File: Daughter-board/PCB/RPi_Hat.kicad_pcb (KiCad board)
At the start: 2 copper layers, 65 x 56.5 mm, 20 parts, among them J1 Conn_01x05, J2 RPi_GPIO, J3 Conn_01x05, J4 Conn_01x05, J5 Conn_01x07, J6 Conn_01x07, J7 Conn_01x05, J8 Conn_02x07_Odd_Even, J9 Conn_01x04, Q1 2N7002, Q2 2N7002, Q3 2N7002

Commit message: update psu and hat
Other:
- board text added: "Hydro B. HAT"
- board text added: "Hydro B. PSU"
- board text removed: "PSU"
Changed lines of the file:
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@@
-(kicad_pcb (version 20171130) (host pcbnew 5.0.2+dfsg1-1~bpo9+1)
+(kicad_pcb (version 20171130) (host pcbnew "(5.1.5)-3")
   (general
     (thickness 1.6)
-    (drawings 37)
+    (drawings 38)
     (tracks 145)
     (zones 0)
@@
     (zone_45_only no)
     (trace_min 0)
-    (segment_width 0.2)
-    (edge_width 0.1)
     (via_size 0.6)
     (via_drill 0.4)
@@
     (uvia_min_size 0.2)
     (uvia_min_drill 0.1)
+    (edge_width 0.1)
+    (segment_width 0.2)
     (pcb_text_width 0.3)
     (pcb_text_size 1.5 1.5)
@@
       (solder_mask_margin 1.725) (clearance 1.725))
   )
-  (gr_text PSU (at 149.86 80.01 90) (layer F.SilkS)
+  (gr_text "Hydro B. HAT" (at 135.255 118.745) (layer F.SilkS)
+    (effects (font (size 3 3) (thickness 0.5)))
+  )
+  (gr_text "Hydro B. PSU" (at 149.86 83.82 90) (layer F.SilkS)
     (effects (font (size 1 1) (thickness 0.15)))
   )
-  (gr_text I2C (at 142.875 111.76 90) (layer F.SilkS)
+  (gr_text I2C (at 142.875 98.425 90) (layer F.SilkS)
     (effects (font (size 1 1) (thickness 0.15)))
   )
-  (gr_text I2C (at 135.255 111.76 90) (layer F.SilkS)
+  (gr_text I2C (at 135.255 98.425 90) (layer F.SilkS)
     (effects (font (size 1 1) (thickness 0.15)))
   )
-  (gr_text I2C (at 127.635 111.76 90) (layer F.SilkS)
+  (gr_text I2C (at 127.635 98.425 90) (layer F.SilkS)
     (effects (font (size 1 1) (thickness 0.15)))
   )

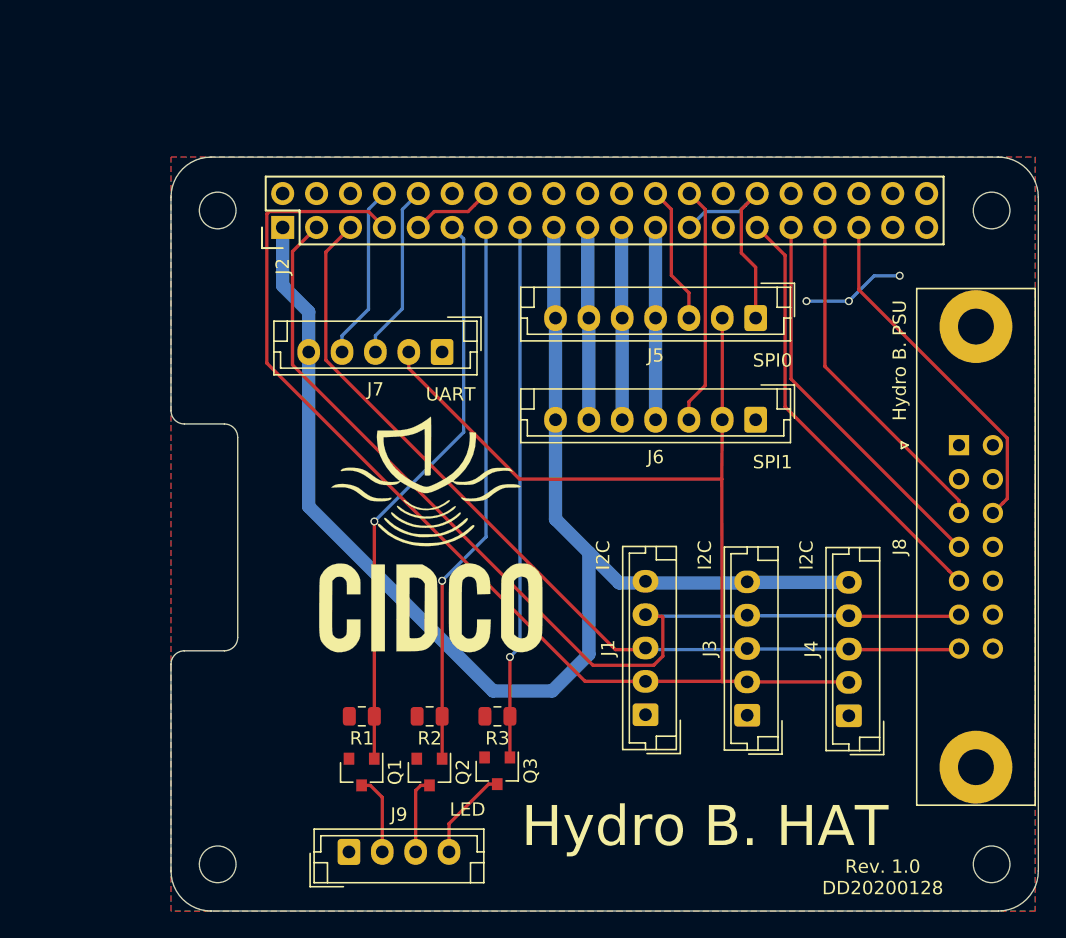
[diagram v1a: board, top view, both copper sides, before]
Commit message: smt to TH
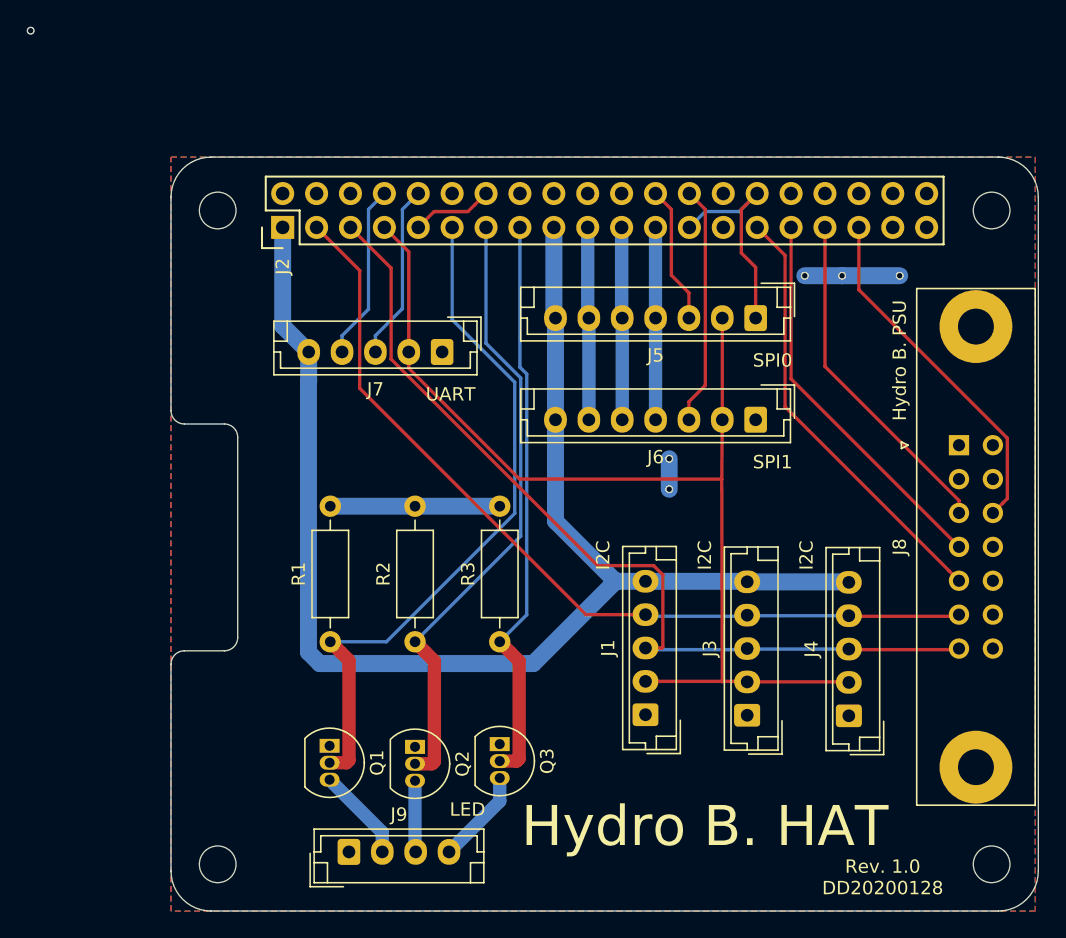
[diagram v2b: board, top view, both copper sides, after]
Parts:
- removed the ? at (156.8, 72.6)
- removed the ? at (156.8, 121.6)
- removed the ? at (98.8, 121.6)
- removed the ? at (98.8, 72.6)
- removed G***: LOGO, cidco:logo cidco
- added ?: , cidco:MountingHole_2.7mm_M2.5_Pad, F.Cu at (98.8, 121.6)
- added ?: , cidco:MountingHole_2.7mm_M2.5_Pad, F.Cu at (156.8, 121.6)
- added ?: , cidco:MountingHole_2.7mm_M2.5_Pad, F.Cu at (156.8, 72.6)
- added ?: , cidco:MountingHole_2.7mm_M2.5_Pad, F.Cu at (98.8, 72.6)
- J2: footprint RPi_Hat:Pin_Header_Straight_2x20 -> cidco:Pin_Header_Straight_2x20
- Q1, Q2, Q3: value 2N7002 -> 2N7000; footprint Package_TO_SOT_SMD:SOT-23 -> Package_TO_SOT_THT:TO-92_Inline
- R1, R2, R3: value R_US -> 1k; footprint Resistor_SMD:R_0805_2012Metric -> Resistor_THT:R_Axial_DIN0207_L6.3mm_D2.5mm_P10.16mm_Horizontal
- moved R1 6.07 mm to (107.2, 104.9), turned to 90 degrees
- moved R2 5.69 mm to (113.5, 104.9), turned to 90 degrees
- moved R3 5.59 mm to (119.9, 104.9), turned to 90 degrees
- moved Q1 3.10 mm to (107.1, 112.7)
- moved Q2 2.18 mm to (113.5, 112.8)
- moved Q3 2.01 mm to (119.9, 112.6)
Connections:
- Q1 pad 1: LEDR -> GND
- Q1 pad 2: GND -> LEDR
- Q2 pad 1: LEDG -> GND
- Q2 pad 2: GND -> LEDG
- Q3 pad 1: LEDB -> GND
- Q3 pad 2: GND -> LEDB
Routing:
- net PPS: track 129.5 -> 80.7 mm
- net GND: track 30.3 -> 44.6 mm, vias 3 -> 5
- net SDA: track 76.2 -> 65.4 mm
- net LEDR: track 42.9 -> 52.2 mm, vias 1 -> 0
- net LEDG: track 41.2 -> 46.5 mm, vias 1 -> 0
- net LEDB: track 40.0 -> 43.0 mm, vias 1 -> 0
- net 3.3V: track 103.1 -> 104.5 mm
- net SCL: track 67.2 -> 68.5 mm
- net Net-(J9-Pad2): track 6.01 -> 7.05 mm
- net (no net): vias 0 -> 1

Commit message: update
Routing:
- net (no net): vias 1 -> 0
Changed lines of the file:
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@@
-(kicad_pcb (version 20171130) (host pcbnew "(5.1.5)-3")
+(kicad_pcb (version 20171130) (host pcbnew 5.0.2+dfsg1-1~bpo9+1)
   (general
     (thickness 1.6)
     (drawings 38)
-    (tracks 152)
+    (tracks 151)
     (zones 0)
     (modules 19)
@@
   )
   (setup
-    (last_trace_width 1.27)
+    (last_trace_width 0.25)
     (user_trace_width 0.01)
     (user_trace_width 0.02)
@@
     (zone_45_only no)
     (trace_min 0)
+    (segment_width 0.2)
+    (edge_width 0.1)
     (via_size 0.6)
     (via_drill 0.4)
@@
     (uvia_min_size 0.2)
     (uvia_min_drill 0.1)
-    (edge_width 0.1)
-    (segment_width 0.2)
     (pcb_text_width 0.3)
     (pcb_text_size 1.5 1.5)
@@
       (rotate (xyz 0 0 90))
     )
+    (model ${KISYS3DMOD}/Connector_PinSocket_2.54mm.3dshapes/PinSocket_2x20_P2.54mm_Vertical.wrl
+      (offset (xyz -1.25 24.15 0))
+      (scale (xyz 1 1 1))
+      (rotate (xyz 0 -180 0))
+    )
   )
   (module Connector_JST:JST_EH_B4B-EH-A_1x04_P2.50mm_Vertical (layer F.Cu)
@@
     (pad "" thru_hole circle (at 1.27 -8.89 270) (size 5.46 5.46) (drill 2.69) (layers *.Cu *.Mask))
     (model ${KISYS3DMOD}/Connector_IDC.3dshapes/IDC-Header_2x07_P2.54mm_Vertical_Lock.wrl
+      (at (xyz 0 0 0))
+      (scale (xyz 1 1 1))
+      (rotate (xyz 0 0 0))
+    )
+    (model ${KISYS3DMOD}/Connector_IDC.3dshapes/IDC-Header_2x07_P2.54mm_Vertical.step
       (at (xyz 0 0 0))
       (scale (xyz 1 1 1))
@@
   (gr_line (start 98.25 125.08) (end 157.25 125.08) (angle 90) (layer Edge.Cuts) (width 0.1))
   (gr_line (start 160.25 71.58) (end 160.25 122.08) (angle 90) (layer Edge.Cuts) (width 0.1))
-  (via (at 84.7344 59.1058) (size 0.6) (drill 0.4) (layers F.Cu B.Cu) (net 0))
   (segment (start 103.62 81.235) (end 105.57 83.185) (width 1.27) (layer B.Cu) (net 1))
   (segment (start 103.62 73.85) (end 103.62 81.235) (width 1.27) (layer B.Cu) (net 1))
@@
   (segment (start 154.185 102.99) (end 154.305 102.87) (width 0.25) (layer F.Cu) (net 3))
   (segment (start 146.05 102.99) (end 154.185 102.99) (width 0.25) (layer F.Cu) (net 3))
+  (segment (start 129.585 102.87) (end 130.81 102.87) (width 0.25) (layer F.Cu) (net 3))
+  (segment (start 126.350998 102.87) (end 129.585 102.87) (width 0.25) (layer F.Cu) (net 3))
+  (segment (start 109.39499 85.913992) (end 126.350998 102.87) (width 0.25) (layer F.Cu) (net 3))
+  (segment (start 109.39499 77.08499) (end 109.39499 85.913992) (width 0.25) (layer F.Cu) (net 3))
+  (segment (start 106.16 73.85) (end 109.39499 77.08499) (width 0.25) (layer F.Cu) (net 3))
   (segment (start 138.39 105.49) (end 138.43 105.45) (width 0.25) (layer B.Cu) (net 4))
   (segment (start 130.81 105.49) (end 138.39 105.49) (width 0.25) (layer B.Cu) (net 4))
@@
   (segment (start 154.225 105.49) (end 154.305 105.41) (width 0.25) (layer F.Cu) (net 4))
   (segment (start 146.05 105.49) (end 154.225 105.49) (width 0.25) (layer F.Cu) (net 4))
+  (segment (start 132.035 105.37) (end 130.81 105.37) (width 0.25) (layer F.Cu) (net 4))
+  (segment (start 132.11001 105.29499) (end 132.035 105.37) (width 0.25) (layer F.Cu) (net 4))
+  (segment (start 132.11001 99.883295) (end 132.11001 105.29499) (width 0.25) (layer F.Cu) (net 4))
+  (segment (start 131.421705 99.19499) (end 132.11001 99.883295) (width 0.25) (layer F.Cu) (net 4))
+  (segment (start 127.21858 99.19499) (end 131.421705 99.19499) (width 0.25) (layer F.Cu) (net 4))
+  (segment (start 111.74501 76.89501) (end 111.74501 83.72142) (width 0.25) (layer F.Cu) (net 4))
+  (segment (start 111.74501 83.72142) (end 127.21858 99.19499) (width 0.25) (layer F.Cu) (net 4))
+  (segment (start 108.7 73.85) (end 111.74501 76.89501) (width 0.25) (layer F.Cu) (net 4))
   (segment (start 117.996401 72.173599) (end 118.86 71.31) (width 0.25) (layer F.Cu) (net 5))
   (segment (start 117.508601 72.661399) (end 117.996401 72.173599) (width 0.25) (layer F.Cu) (net 5))
@@
   (segment (start 139.065 76.835) (end 139.065 80.645) (width 0.25) (layer F.Cu) (net 5))
   (segment (start 137.991399 75.761399) (end 139.065 76.835) (width 0.25) (layer F.Cu) (net 5))
-  (segment (start 129.585 102.87) (end 130.81 102.87) (width 0.25) (layer F.Cu) (net 3))
-  (segment (start 126.350998 102.87) (end 129.585 102.87) (width 0.25) (layer F.Cu) (net 3))
-  (segment (start 109.39499 85.913992) (end 126.350998 102.87) (width 0.25) (layer F.Cu) (net 3))
-  (segment (start 109.39499 77.08499) (end 109.39499 85.913992) (width 0.25) (layer F.Cu) (net 3))
-  (segment (start 106.16 73.85) (end 109.39499 77.08499) (width 0.25) (layer F.Cu) (net 3))
-  (segment (start 132.035 105.37) (end 130.81 105.37) (width 0.25) (layer F.Cu) (net 4))
-  (segment (start 132.11001 105.29499) (end 132.035 105.37) (width 0.25) (layer F.Cu) (net 4))
-  (segment (start 132.11001 99.883295) (end 132.11001 105.29499) (width 0.25) (layer F.Cu) (net 4))
-  (segment (start 131.421705 99.19499) (end 132.11001 99.883295) (width 0.25) (layer F.Cu) (net 4))
-  (segment (start 127.21858 99.19499) (end 131.421705 99.19499) (width 0.25) (layer F.Cu) (net 4))
-  (segment (start 111.74501 76.89501) (end 111.74501 83.72142) (width 0.25) (layer F.Cu) (net 4))
-  (segment (start 111.74501 83.72142) (end 127.21858 99.19499) (width 0.25) (layer F.Cu) (net 4))
-  (segment (start 108.7 73.85) (end 111.74501 76.89501) (width 0.25) (layer F.Cu) (net 4))
   (segment (start 107.188 94.742) (end 113.538 94.742) (width 1.27) (layer B.Cu) (net 5))
   (segment (start 113.538 94.742) (end 119.888 94.742) (width 1.27) (layer B.Cu) (net 5))

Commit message: update hat
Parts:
- added G***: LOGO, cidco:logo cidco, F.Cu at (113.0, 94.6)
- R1, R2, R3: footprint Resistor_THT:R_Axial_DIN0207_L6.3mm_D2.5mm_P10.16mm_Horizontal -> Resistor_THT:R_Axial_DIN0207_L6.3mm_D2.5mm_P2.54mm_Vertical
- moved R1 4.50 mm to (107.2, 109.4)
- moved R2 4.50 mm to (113.6, 109.4)
- moved R3 4.45 mm to (119.9, 109.3)
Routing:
- net 3.3V: track 104.5 -> 89.8 mm, vias 0 -> 2
- net GND: track 44.6 -> 31.9 mm
- net LEDR: track 52.2 -> 46.1 mm
- net LEDG: track 46.5 -> 43.9 mm
- net LEDB: track 43.0 -> 42.1 mm

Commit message: update
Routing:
- net GND: track 31.9 -> 33.1 mm
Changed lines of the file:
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@@
-(kicad_pcb (version 20171130) (host pcbnew "(5.1.5)-3")
+(kicad_pcb (version 20171130) (host pcbnew 5.0.2+dfsg1-1~bpo9+1)
   (general
     (thickness 1.6)
@@
     (zone_45_only no)
     (trace_min 0)
+    (segment_width 0.2)
+    (edge_width 0.1)
     (via_size 0.6)
     (via_drill 0.4)
@@
     (uvia_min_size 0.2)
     (uvia_min_drill 0.1)
-    (edge_width 0.1)
-    (segment_width 0.2)
     (pcb_text_width 0.3)
     (pcb_text_size 1.5 1.5)
@@
   (segment (start 139.065 76.835) (end 139.065 80.645) (width 0.25) (layer F.Cu) (net 5))
   (segment (start 137.991399 75.761399) (end 139.065 76.835) (width 0.25) (layer F.Cu) (net 5))
-  (via (at 132.588 91.186) (size 0.6) (drill 0.4) (layers F.Cu B.Cu) (net 5))
-  (via (at 132.588 93.472) (size 0.6) (drill 0.4) (layers F.Cu B.Cu) (net 5))
-  (segment (start 132.588 91.186) (end 132.588 93.472) (width 1.27) (layer B.Cu) (net 5))
+  (via (at 133.35 91.186) (size 0.6) (drill 0.4) (layers F.Cu B.Cu) (net 5))
+  (via (at 133.35 94.615) (size 0.6) (drill 0.4) (layers F.Cu B.Cu) (net 5))
   (via (at 149.86 77.47) (size 0.6) (drill 0.4) (layers F.Cu B.Cu) (net 5))
   (via (at 145.542 77.47) (size 0.6) (drill 0.4) (layers F.Cu B.Cu) (net 5))
@@
   (segment (start 149.86 77.47) (end 145.542 77.47) (width 1.27) (layer B.Cu) (net 5))
   (segment (start 145.542 77.47) (end 142.748 77.47) (width 1.27) (layer B.Cu) (net 5))
+  (segment (start 133.35 91.186) (end 133.35 94.615) (width 1.27) (layer B.Cu) (net 5))
   (segment (start 138.39 107.87) (end 138.43 107.91) (width 0.25) (layer F.Cu) (net 6))
   (segment (start 130.81 107.87) (end 138.39 107.87) (width 0.25) (layer F.Cu) (net 6))
